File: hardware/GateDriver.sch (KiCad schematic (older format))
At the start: 0 parts

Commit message: Updaated Driver section
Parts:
- added C1, C2, C3: 0.1u, symbol C
- added C4, C5, C6: 1.0u, symbol C
- added PhaseA, PhaseB, PhaseC: UCC2720xA, symbol UCC2720xA
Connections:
- new net: C1.1, PhaseA.2 (HB)
- new net: C2.1, PhaseB.2 (HB)
- new net: C3.1, PhaseC.2 (HB)
- new net +12V: C4.2, C5.2, C6.2, PhaseA.1 (VDD), PhaseB.1 (VDD), PhaseC.1 (VDD)
- new net GND: C4.1, C5.1, C6.1, PhaseA.7 (VSS), PhaseB.7 (VSS), PhaseC.7 (VSS)
- new net HS_A_GATE: PhaseA.3 (HO)
- new net HS_A_TTL_PWM: PhaseA.5 (HI)
- new net HS_B_GATE: PhaseB.3 (HO)
- new net HS_B_TTL_PWM: PhaseB.5 (HI)
- new net HS_C_GATE: PhaseC.3 (HO)
- new net HS_C_TTL_PWM: PhaseC.5 (HI)
- new net LS_A_GATE: PhaseA.8 (LO)
- new net LS_A_TTL_PWM: PhaseA.6 (LI)
- new net LS_B_GATE: PhaseB.8 (LO)
- new net LS_B_TTL_PWM: PhaseB.6 (LI)
- new net LS_C_GATE: PhaseC.8 (LO)
- new net LS_C_TTL_PWM: PhaseC.6 (LI)
- new net PhaseA: C1.2, PhaseA.4 (HS)
- new net PhaseB: C2.2, PhaseB.4 (HS)
- new net PhaseC: C3.2, PhaseC.4 (HS)
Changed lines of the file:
@@
 LIBS:valves
 LIBS:infineon
+LIBS:bldc_v1-cache
 EELAYER 25 0
 EELAYER END
@@
 encoding utf-8
 Sheet 2 3
-Title ""
-Date ""
-Rev ""
-Comp ""
+Title "Gate Drivers"
+Date "2018-03-18"
+Rev "1"
+Comp "Loma Incorporated"
 Comment1 ""
 Comment2 ""
@@
 Comment4 ""
 $EndDescr
+$Comp
+L UCC2720xA PhaseA
+U 1 1 5AAF1479
+P 3800 1900
+F 0 "PhaseA" H 3900 1500 60  0000 C CNN
+F 1 "UCC2720xA" H 3900 2100 60  0000 C CNN
+F 2 "" H 3800 1900 60  0001 C CNN
+F 3 "" H 3800 1900 60  0001 C CNN
+	1    3800 1900
+	1    0    0    -1
+$EndComp
+$Comp
+L UCC2720xA PhaseB
+U 1 1 5AAF151B
+P 3800 3000
+F 0 "PhaseB" H 3900 2600 60  0000 C CNN
+F 1 "UCC2720xA" H 3900 3200 60  0000 C CNN
+F 2 "" H 3800 3000 60  0001 C CNN
+F 3 "" H 3800 3000 60  0001 C CNN
+	1    3800 3000
+	1    0    0    -1
+$EndComp
+$Comp
+L UCC2720xA PhaseC
+U 1 1 5AAF1572
+P 3800 4150
+F 0 "PhaseC" H 3900 3750 60  0000 C CNN
+F 1 "UCC2720xA" H 3900 4350 60  0000 C CNN
+F 2 "" H 3800 4150 60  0001 C CNN
+F 3 "" H 3800 4150 60  0001 C CNN
+	1    3800 4150
+	1    0    0    -1
+$EndComp
+$Comp
+L C C1
+U 1 1 5AAF19CF
+P 2450 2100
+F 0 "C1" H 2475 2200 50  0000 L CNN
+F 1 "0.1u" H 2475 2000 50  0000 L CNN
+F 2 "" H 2488 1950 50  0001 C CNN
+F 3 "" H 2450 2100 50  0001 C CNN
+	1    2450 2100
+	1    0    0    -1
+$EndComp
+$Comp
+L C C2
+U 1 1 5AAF1A5A
+P 2400 3200
+F 0 "C2" H 2425 3300 50  0000 L CNN
+F 1 "0.1u" H 2425 3100 50  0000 L CNN
+F 2 "" H 2438 3050 50  0001 C CNN
+F 3 "" H 2400 3200 50  0001 C CNN
+	1    2400 3200
+	1    0    0    -1
+$EndComp
+$Comp
+L C C3
+U 1 1 5AAF1AF9
+P 2400 4350
+F 0 "C3" H 2425 4450 50  0000 L CNN
+F 1 "0.1u" H 2425 4250 50  0000 L CNN
+F 2 "" H 2438 4200 50  0001 C CNN
+F 3 "" H 2400 4350 50  0001 C CNN
+	1    2400 4350
+	1    0    0    -1
+$EndComp
+Text HLabel 2250 2250 0    60   Input ~ 0
+PhaseA
+Text HLabel 2250 3350 0    60   Input ~ 0
+PhaseB
+Text HLabel 2250 4500 0    60   Input ~ 0
+PhaseC
+Text HLabel 5100 900  0    60   Input ~ 0
+GND
+Text HLabel 4400 1850 2    60   Output ~ 0
+LS_A_GATE
+Text HLabel 3350 2050 0    60   Output ~ 0
+HS_A_GATE
+Wire Wire Line
+	3500 2050 3350 2050
+Wire Wire Line
+	2250 2250 2900 2250
+Wire Wire Line
+	3500 2150 2900 2150
+Wire Wire Line
+	2900 2150 2900 2250
+Connection ~ 2450 2250
+Wire Wire Line
+	2450 1950 3500 1950
+Wire Wire Line
+	4300 1850 4400 1850
+Text HLabel 4450 2950 2    60   Output ~ 0
+LS_B_GATE
+Wire Wire Line
+	4300 2950 4450 2950
+Connection ~ 2400 3350
+Wire Wire Line
+	2400 3050 3500 3050
+Wire Wire Line
+	2250 4500 2850 4500
+Wire Wire Line
+	2850 4500 2850 4400
+Wire Wire Line
+	2850 4400 3500 4400
+Connection ~ 2400 4500
+Wire Wire Line
+	2400 4200 3500 4200
+Wire Wire Line
+	2250 3350 2750 3350
+Wire Wire Line
+	2750 3350 2750 3250
+Wire Wire Line
+	2750 3250 3500 3250
+Text HLabel 3350 3150 0    60   Output ~ 0
+HS_B_GATE
+Wire Wire Line
+	3350 3150 3500 3150
+Text HLabel 4450 4100 2    60   Output ~ 0
+LS_C_GATE
+Text HLabel 3350 4300 0    60   Output ~ 0
+HS_C_GATE
+Wire Wire Line
+	3500 4300 3350 4300
+Wire Wire Line
+	4300 4100 4450 4100
+Wire Wire Line
+	5300 900  5300 4200
+Wire Wire Line
+	5300 1950 4300 1950
+Wire Wire Line
+	5300 3050 4300 3050
+Connection ~ 5300 1950
+Wire Wire Line
+	5300 4200 4300 4200
+Connection ~ 5300 3050
+$Comp
+L C C4
+U 1 1 5AAF26C0
+P 3900 1300
+F 0 "C4" H 3925 1400 50  0000 L CNN
+F 1 "1.0u" H 3925 1200 50  0000 L CNN
+F 2 "" H 3938 1150 50  0001 C CNN
+F 3 "" H 3900 1300 50  0001 C CNN
+	1    3900 1300
+	0    1    1    0
+$EndComp
+Wire Wire Line
+	5300 900  5100 900
+Wire Wire Line
+	4050 1300 5300 1300
+Connection ~ 5300 1300
+Wire Wire Line
+	2950 1300 3750 1300
+Wire Wire Line
+	3500 950  3500 1850
+$Comp
+L C C5
+U 1 1 5AAF28D3
+P 3950 2500
+F 0 "C5" H 3975 2600 50  0000 L CNN
+F 1 "1.0u" H 3975 2400 50  0000 L CNN
+F 2 "" H 3988 2350 50  0001 C CNN
+F 3 "" H 3950 2500 50  0001 C CNN
+	1    3950 2500
+	0    1    1    0
+$EndComp
+Wire Wire Line
+	4100 2500 5300 2500
+Connection ~ 5300 2500
+Wire Wire Line
+	3150 2500 3800 2500
+Wire Wire Line
+	3500 2500 3500 2950
+$Comp
+L C C6
+U 1 1 5AAF29AA
+P 3950 3650
+F 0 "C6" H 3975 3750 50  0000 L CNN
+F 1 "1.0u" H 3975 3550 50  0000 L CNN
+F 2 "" H 3988 3500 50  0001 C CNN
+F 3 "" H 3950 3650 50  0001 C CNN
+	1    3950 3650
+	0    1    1    0
+$EndComp
+Wire Wire Line
+	4100 3650 5300 3650
+Connection ~ 5300 3650
+Wire Wire Line
+	3500 4100 3500 3650
+Wire Wire Line
+	3150 3650 3800 3650
+Text HLabel 4400 2050 2    60   Input ~ 0
+LS_A_TTL_PWM
+Wire Wire Line
+	4300 2050 4400 2050
+Text HLabel 4400 2150 2    60   Input ~ 0
+HS_A_TTL_PWM
+Wire Wire Line
+	4400 2150 4300 2150
+Text HLabel 4450 3150 2    60   Input ~ 0
+LS_B_TTL_PWM
+Wire Wire Line
+	4450 3150 4300 3150
+Text HLabel 4450 3250 2    60   Input ~ 0
+HS_B_TTL_PWM
+Wire Wire Line
+	4450 3250 4300 3250
+Text HLabel 4450 4300 2    60   Input ~ 0
+LS_C_TTL_PWM
+Wire Wire Line
+	4300 4300 4450 4300
+Text HLabel 4450 4400 2    60   Input ~ 0
+HS_C_TTL_PWM
+Wire Wire Line
+	4300 4400 4450 4400
+Text HLabel 2950 1300 0    60   Input ~ 0
++12V
+Connection ~ 3500 1300
+Wire Wire Line
+	3650 950  3500 950
+Connection ~ 3500 2500
+Connection ~ 3500 3650
+Text Label 3650 950  0    60   ~ 0
++12V
+Text Label 3150 2500 0    60   ~ 0
++12V
+Text Label 3150 3650 0    60   ~ 0
++12V
 $EndSCHEMATC

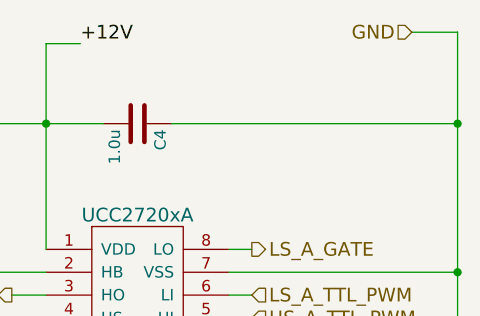
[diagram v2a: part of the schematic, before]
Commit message: Added power converters
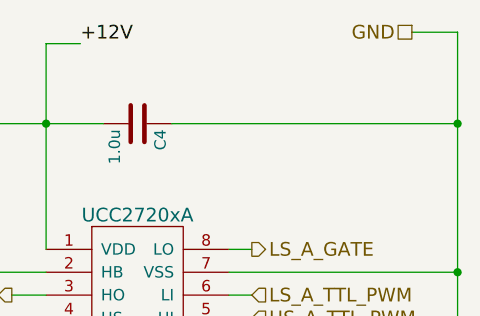
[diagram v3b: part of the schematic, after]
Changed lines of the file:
@@
 $Descr A4 11693 8268
 encoding utf-8
-Sheet 2 3
+Sheet 2 4
 Title "Gate Drivers"
 Date "2018-03-18"
@@
 Text HLabel 2250 4500 0    60   Input ~ 0
 PhaseC
-Text HLabel 5100 900  0    60   Input ~ 0
+Text HLabel 5100 900  0    60   UnSpc ~ 0
 GND
 Text HLabel 4400 1850 2    60   Output ~ 0

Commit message: added microcontroller page
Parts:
- C1, C2, C3: PN (none) -> TMK105BJ104KV-F
- C4, C5, C6: PN (none) -> CC0805KKX7R8BB105
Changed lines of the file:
@@
 LIBS:valves
 LIBS:infineon
+LIBS:crf_1
+LIBS:STM32F4-DISCOVERY-SIMON
+LIBS:bldc_v1-cache
 EELAYER 25 0
 EELAYER END
 $Descr A4 11693 8268
 encoding utf-8
-Sheet 2 4
+Sheet 2 5
 Title "Gate Drivers"
 Date "2018-03-18"
@@
 F 2 "" H 2488 1950 50  0001 C CNN
 F 3 "" H 2450 2100 50  0001 C CNN
+F 4 "TMK105BJ104KV-F " H 1950 2100 60  0000 C CNN "PN"
 	1    2450 2100
 	1    0    0    -1
@@
 F 2 "" H 2438 3050 50  0001 C CNN
 F 3 "" H 2400 3200 50  0001 C CNN
+F 4 "TMK105BJ104KV-F " H 1900 3200 60  0000 C CNN "PN"
 	1    2400 3200
 	1    0    0    -1
@@
 F 2 "" H 2438 4200 50  0001 C CNN
 F 3 "" H 2400 4350 50  0001 C CNN
+F 4 "TMK105BJ104KV-F " H 1900 4350 60  0000 C CNN "PN"
 	1    2400 4350
 	1    0    0    -1
@@
 F 2 "" H 3938 1150 50  0001 C CNN
 F 3 "" H 3900 1300 50  0001 C CNN
+F 4 "CC0805KKX7R8BB105 " V 3750 1550 60  0000 C CNN "PN"
 	1    3900 1300
 	0    1    1    0
@@
 F 2 "" H 3988 2350 50  0001 C CNN
 F 3 "" H 3950 2500 50  0001 C CNN
+F 4 "CC0805KKX7R8BB105 " V 3900 3100 60  0000 C CNN "PN"
 	1    3950 2500
 	0    1    1    0
@@
 F 2 "" H 3988 3500 50  0001 C CNN
 F 3 "" H 3950 3650 50  0001 C CNN
+F 4 "CC0805KKX7R8BB105 " V 3900 4200 60  0000 C CNN "PN"
 	1    3950 3650
 	0    1    1    0

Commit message: associated footprints
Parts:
- C1, C2, C3: footprint (none) -> Capacitors_SMD:C_0402
- C4, C5, C6: footprint (none) -> Capacitors_SMD:C_0805_HandSoldering
- PhaseA, PhaseB, PhaseC: footprint (none) -> Housings_SOIC:Infineon_PG-DSO-8-43
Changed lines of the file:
@@
 F 0 "PhaseA" H 3900 1500 60  0000 C CNN
 F 1 "UCC2720xA" H 3900 2100 60  0000 C CNN
-F 2 "" H 3800 1900 60  0001 C CNN
+F 2 "Housings_SOIC:Infineon_PG-DSO-8-43" H 3800 1900 60  0001 C CNN
 F 3 "" H 3800 1900 60  0001 C CNN
 	1    3800 1900
@@
 F 0 "PhaseB" H 3900 2600 60  0000 C CNN
 F 1 "UCC2720xA" H 3900 3200 60  0000 C CNN
-F 2 "" H 3800 3000 60  0001 C CNN
+F 2 "Housings_SOIC:Infineon_PG-DSO-8-43" H 3800 3000 60  0001 C CNN
 F 3 "" H 3800 3000 60  0001 C CNN
 	1    3800 3000
@@
 F 0 "PhaseC" H 3900 3750 60  0000 C CNN
 F 1 "UCC2720xA" H 3900 4350 60  0000 C CNN
-F 2 "" H 3800 4150 60  0001 C CNN
+F 2 "Housings_SOIC:Infineon_PG-DSO-8-43" H 3800 4150 60  0001 C CNN
 F 3 "" H 3800 4150 60  0001 C CNN
 	1    3800 4150
@@
 F 0 "C1" H 2475 2200 50  0000 L CNN
 F 1 "0.1u" H 2475 2000 50  0000 L CNN
-F 2 "" H 2488 1950 50  0001 C CNN
+F 2 "Capacitors_SMD:C_0402" H 2488 1950 50  0001 C CNN
 F 3 "" H 2450 2100 50  0001 C CNN
 F 4 "TMK105BJ104KV-F " H 1950 2100 60  0000 C CNN "PN"
@@
 F 0 "C2" H 2425 3300 50  0000 L CNN
 F 1 "0.1u" H 2425 3100 50  0000 L CNN
-F 2 "" H 2438 3050 50  0001 C CNN
+F 2 "Capacitors_SMD:C_0402" H 2438 3050 50  0001 C CNN
 F 3 "" H 2400 3200 50  0001 C CNN
 F 4 "TMK105BJ104KV-F " H 1900 3200 60  0000 C CNN "PN"
@@
 F 0 "C3" H 2425 4450 50  0000 L CNN
 F 1 "0.1u" H 2425 4250 50  0000 L CNN
-F 2 "" H 2438 4200 50  0001 C CNN
+F 2 "Capacitors_SMD:C_0402" H 2438 4200 50  0001 C CNN
 F 3 "" H 2400 4350 50  0001 C CNN
 F 4 "TMK105BJ104KV-F " H 1900 4350 60  0000 C CNN "PN"
@@
 F 0 "C4" H 3925 1400 50  0000 L CNN
 F 1 "1.0u" H 3925 1200 50  0000 L CNN
-F 2 "" H 3938 1150 50  0001 C CNN
+F 2 "Capacitors_SMD:C_0805_HandSoldering" H 3938 1150 50  0001 C CNN
 F 3 "" H 3900 1300 50  0001 C CNN
 F 4 "CC0805KKX7R8BB105 " V 3750 1550 60  0000 C CNN "PN"
@@
 F 0 "C5" H 3975 2600 50  0000 L CNN
 F 1 "1.0u" H 3975 2400 50  0000 L CNN
-F 2 "" H 3988 2350 50  0001 C CNN
+F 2 "Capacitors_SMD:C_0805_HandSoldering" H 3988 2350 50  0001 C CNN
 F 3 "" H 3950 2500 50  0001 C CNN
 F 4 "CC0805KKX7R8BB105 " V 3900 3100 60  0000 C CNN "PN"
@@
 F 0 "C6" H 3975 3750 50  0000 L CNN
 F 1 "1.0u" H 3975 3550 50  0000 L CNN
-F 2 "" H 3988 3500 50  0001 C CNN
+F 2 "Capacitors_SMD:C_0805_HandSoldering" H 3988 3500 50  0001 C CNN
 F 3 "" H 3950 3650 50  0001 C CNN
 F 4 "CC0805KKX7R8BB105 " V 3900 4200 60  0000 C CNN "PN"

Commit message: annotated schematic
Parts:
- renumbered C2 to C1, C3 to C2, C1 to C3, PhaseA to PhaseA1, PhaseB to PhaseB1, PhaseC to PhaseC1
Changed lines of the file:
@@
 $EndDescr
 $Comp
-L UCC2720xA PhaseA
+L UCC2720xA PhaseA1
 U 1 1 5AAF1479
 P 3800 1900
-F 0 "PhaseA" H 3900 1500 60  0000 C CNN
+F 0 "PhaseA1" H 3900 1500 60  0000 C CNN
 F 1 "UCC2720xA" H 3900 2100 60  0000 C CNN
 F 2 "Housings_SOIC:Infineon_PG-DSO-8-43" H 3800 1900 60  0001 C CNN
@@
 $EndComp
 $Comp
-L UCC2720xA PhaseB
+L UCC2720xA PhaseB1
 U 1 1 5AAF151B
 P 3800 3000
-F 0 "PhaseB" H 3900 2600 60  0000 C CNN
+F 0 "PhaseB1" H 3900 2600 60  0000 C CNN
 F 1 "UCC2720xA" H 3900 3200 60  0000 C CNN
 F 2 "Housings_SOIC:Infineon_PG-DSO-8-43" H 3800 3000 60  0001 C CNN
@@
 $EndComp
 $Comp
-L UCC2720xA PhaseC
+L UCC2720xA PhaseC1
 U 1 1 5AAF1572
 P 3800 4150
-F 0 "PhaseC" H 3900 3750 60  0000 C CNN
+F 0 "PhaseC1" H 3900 3750 60  0000 C CNN
 F 1 "UCC2720xA" H 3900 4350 60  0000 C CNN
 F 2 "Housings_SOIC:Infineon_PG-DSO-8-43" H 3800 4150 60  0001 C CNN
@@
 $EndComp
 $Comp
-L C C1
+L C C3
 U 1 1 5AAF19CF
 P 2450 2100
-F 0 "C1" H 2475 2200 50  0000 L CNN
+F 0 "C3" H 2475 2200 50  0000 L CNN
 F 1 "0.1u" H 2475 2000 50  0000 L CNN
 F 2 "Capacitors_SMD:C_0402" H 2488 1950 50  0001 C CNN
@@
 $EndComp
 $Comp
-L C C2
+L C C1
 U 1 1 5AAF1A5A
 P 2400 3200
-F 0 "C2" H 2425 3300 50  0000 L CNN
+F 0 "C1" H 2425 3300 50  0000 L CNN
 F 1 "0.1u" H 2425 3100 50  0000 L CNN
 F 2 "Capacitors_SMD:C_0402" H 2438 3050 50  0001 C CNN
@@
 $EndComp
 $Comp
-L C C3
+L C C2
 U 1 1 5AAF1AF9
 P 2400 4350
-F 0 "C3" H 2425 4450 50  0000 L CNN
+F 0 "C2" H 2425 4450 50  0000 L CNN
 F 1 "0.1u" H 2425 4250 50  0000 L CNN
 F 2 "Capacitors_SMD:C_0402" H 2438 4200 50  0001 C CNN

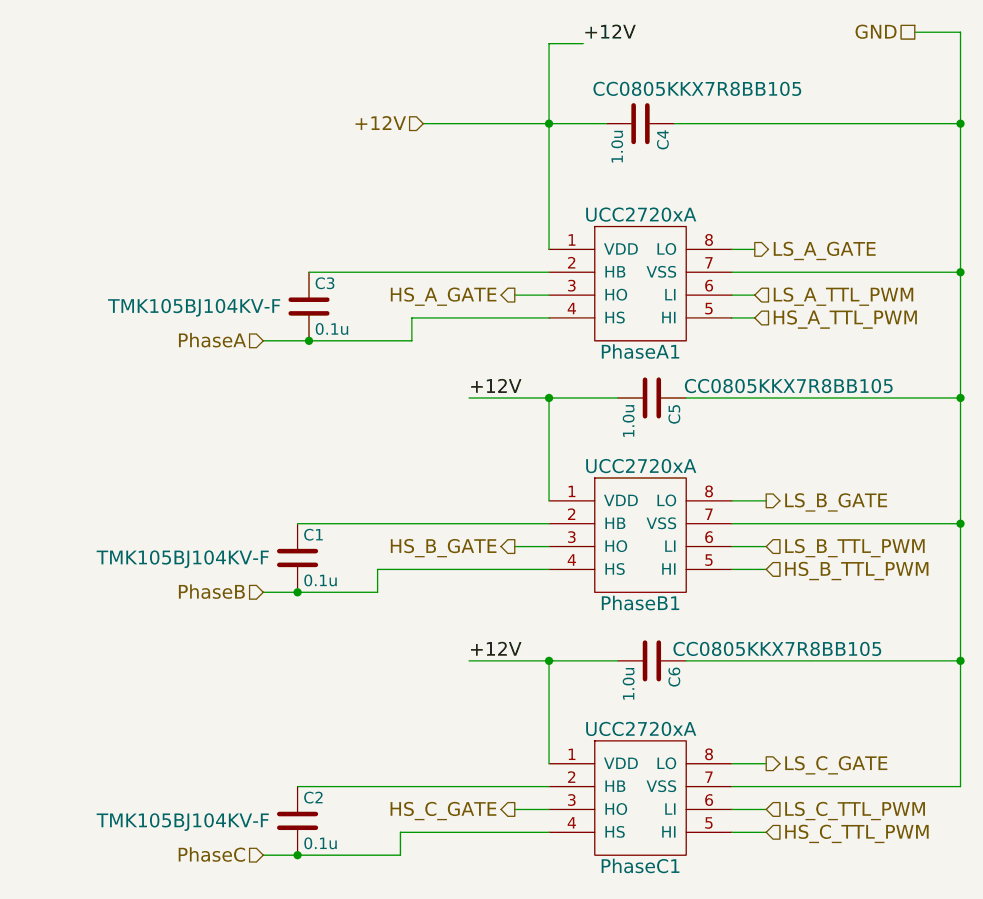
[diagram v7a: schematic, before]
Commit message: layed parts out on board
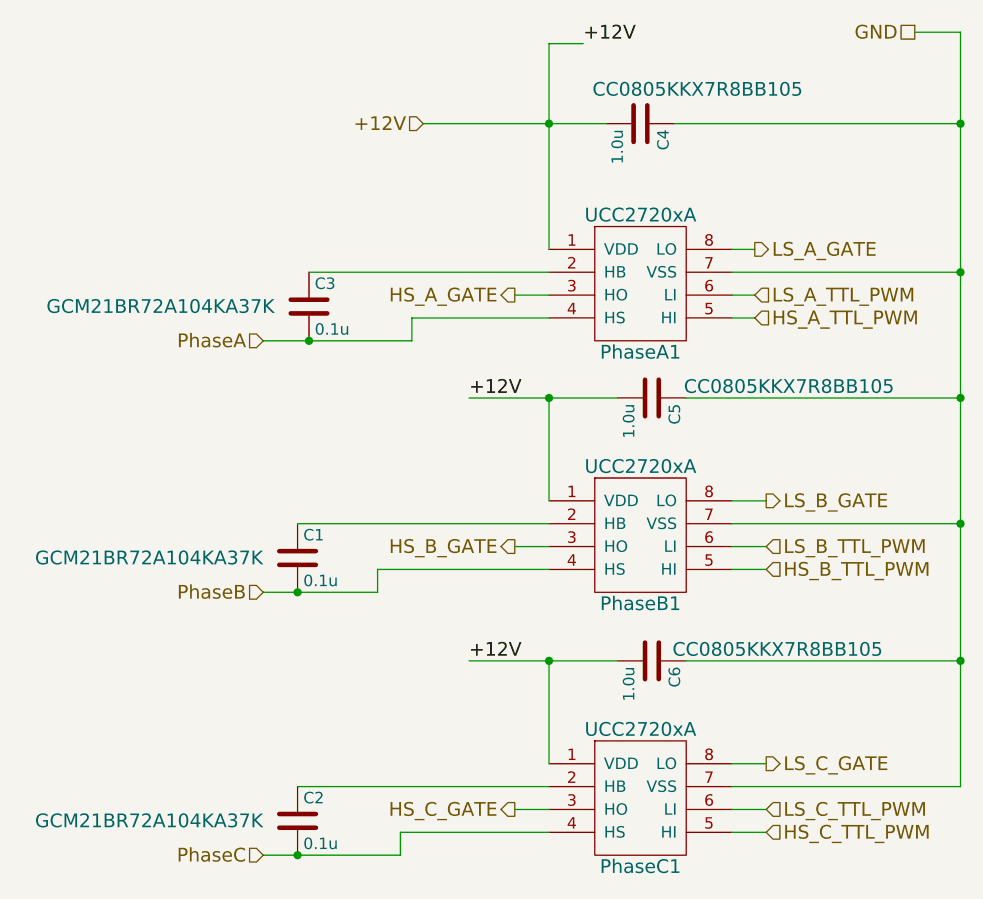
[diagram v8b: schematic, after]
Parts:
- C1, C2, C3: footprint Capacitors_SMD:C_0402 -> Capacitors_SMD:C_0805_HandSoldering; PN TMK105BJ104KV-F -> GCM21BR72A104KA37K
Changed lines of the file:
@@
 LIBS:crf_1
 LIBS:STM32F4-DISCOVERY-SIMON
+LIBS:bldc_v1-cache
 EELAYER 25 0
 EELAYER END
@@
 F 0 "C3" H 2475 2200 50  0000 L CNN
 F 1 "0.1u" H 2475 2000 50  0000 L CNN
-F 2 "Capacitors_SMD:C_0402" H 2488 1950 50  0001 C CNN
+F 2 "Capacitors_SMD:C_0805_HandSoldering" H 2488 1950 50  0001 C CNN
 F 3 "" H 2450 2100 50  0001 C CNN
-F 4 "TMK105BJ104KV-F " H 1950 2100 60  0000 C CNN "PN"
+F 4 "GCM21BR72A104KA37K" H 1800 2100 60  0000 C CNN "PN"
 	1    2450 2100
 	1    0    0    -1
@@
 F 0 "C1" H 2425 3300 50  0000 L CNN
 F 1 "0.1u" H 2425 3100 50  0000 L CNN
-F 2 "Capacitors_SMD:C_0402" H 2438 3050 50  0001 C CNN
+F 2 "Capacitors_SMD:C_0805_HandSoldering" H 2438 3050 50  0001 C CNN
 F 3 "" H 2400 3200 50  0001 C CNN
-F 4 "TMK105BJ104KV-F " H 1900 3200 60  0000 C CNN "PN"
+F 4 "GCM21BR72A104KA37K" H 1750 3200 60  0000 C CNN "PN"
 	1    2400 3200
 	1    0    0    -1
@@
 F 0 "C2" H 2425 4450 50  0000 L CNN
 F 1 "0.1u" H 2425 4250 50  0000 L CNN
-F 2 "Capacitors_SMD:C_0402" H 2438 4200 50  0001 C CNN
+F 2 "Capacitors_SMD:C_0805_HandSoldering" H 2438 4200 50  0001 C CNN
 F 3 "" H 2400 4350 50  0001 C CNN
-F 4 "TMK105BJ104KV-F " H 1900 4350 60  0000 C CNN "PN"
+F 4 "GCM21BR72A104KA37K" H 1750 4350 60  0000 C CNN "PN"
 	1    2400 4350
 	1    0    0    -1
